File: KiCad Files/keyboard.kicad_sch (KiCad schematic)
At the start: 208 parts, among them J1 Conn_01x10, J2 Button, J3 78171-0004, J5 Conn_01x03_Male, U1 SOT-23-5 5.5V 3.3V 500mA, U2 RP2040, U3 TXS0101DCK, Y1 3225_4P 12MHz

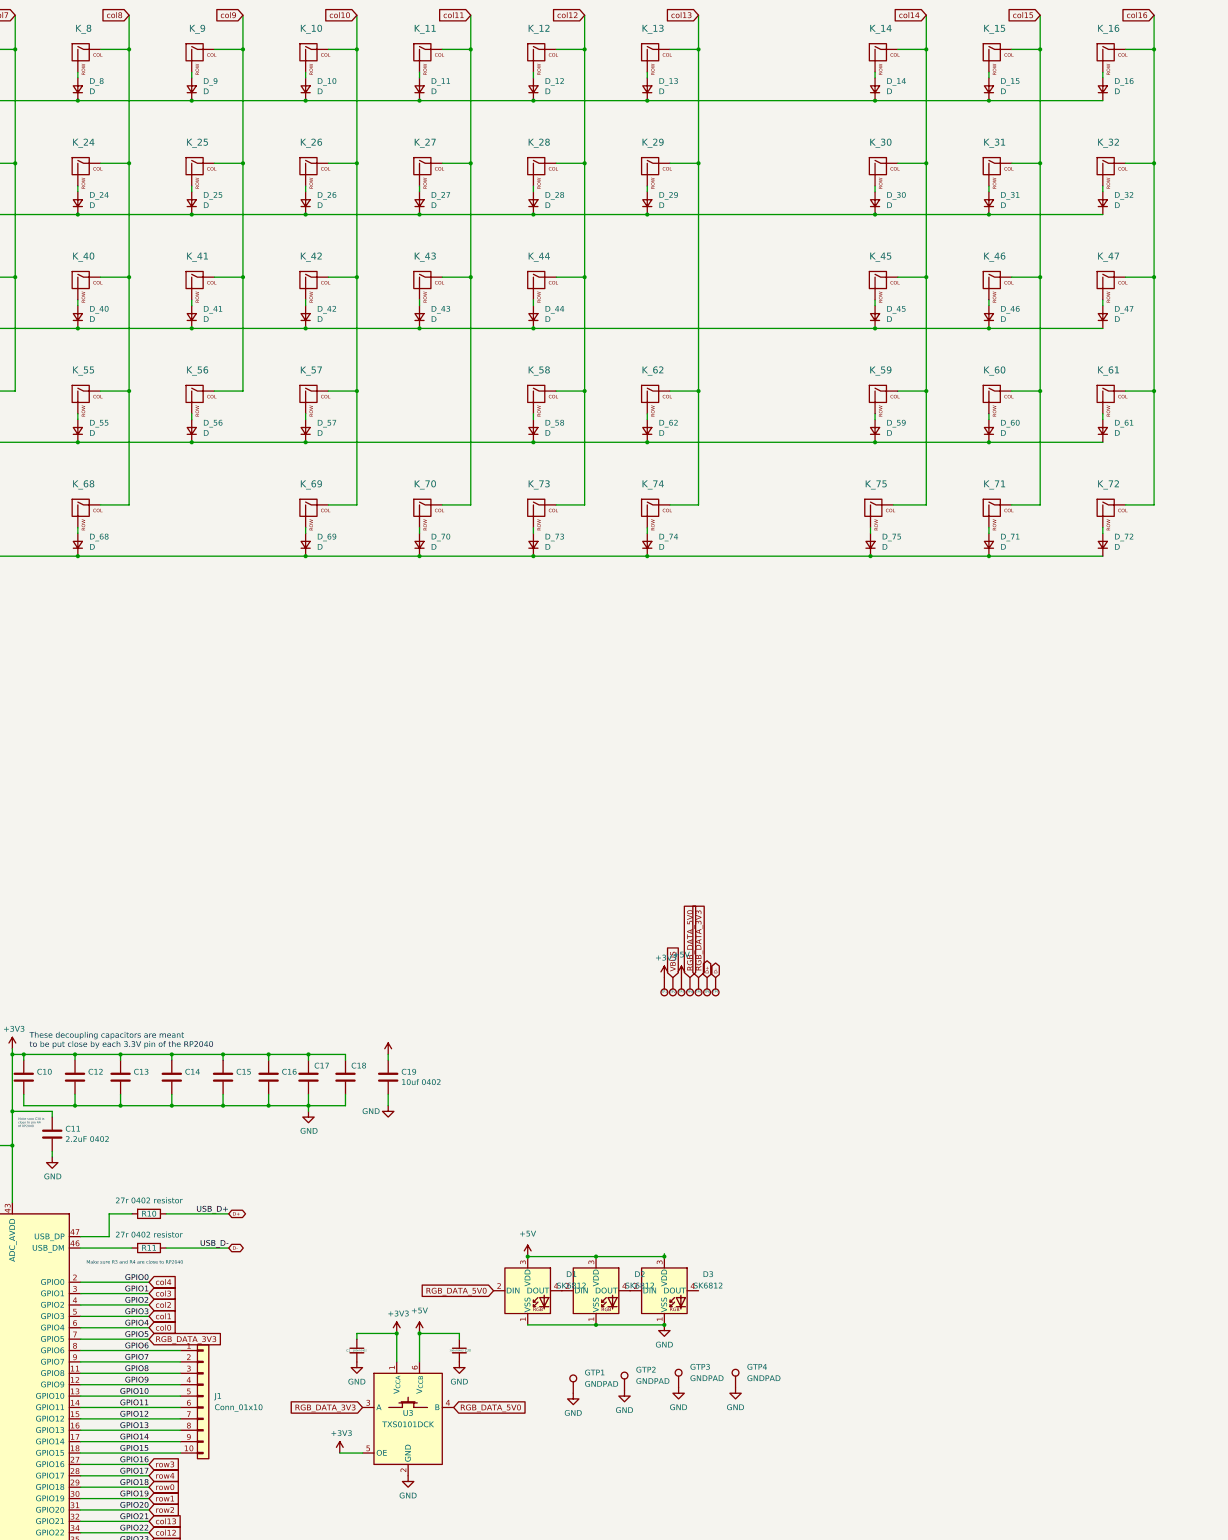
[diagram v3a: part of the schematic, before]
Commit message: corrected two major issues, columns 14,15 and 16 were not connected to any GPIOs, the LED footprints were incorrect for reverse mount.
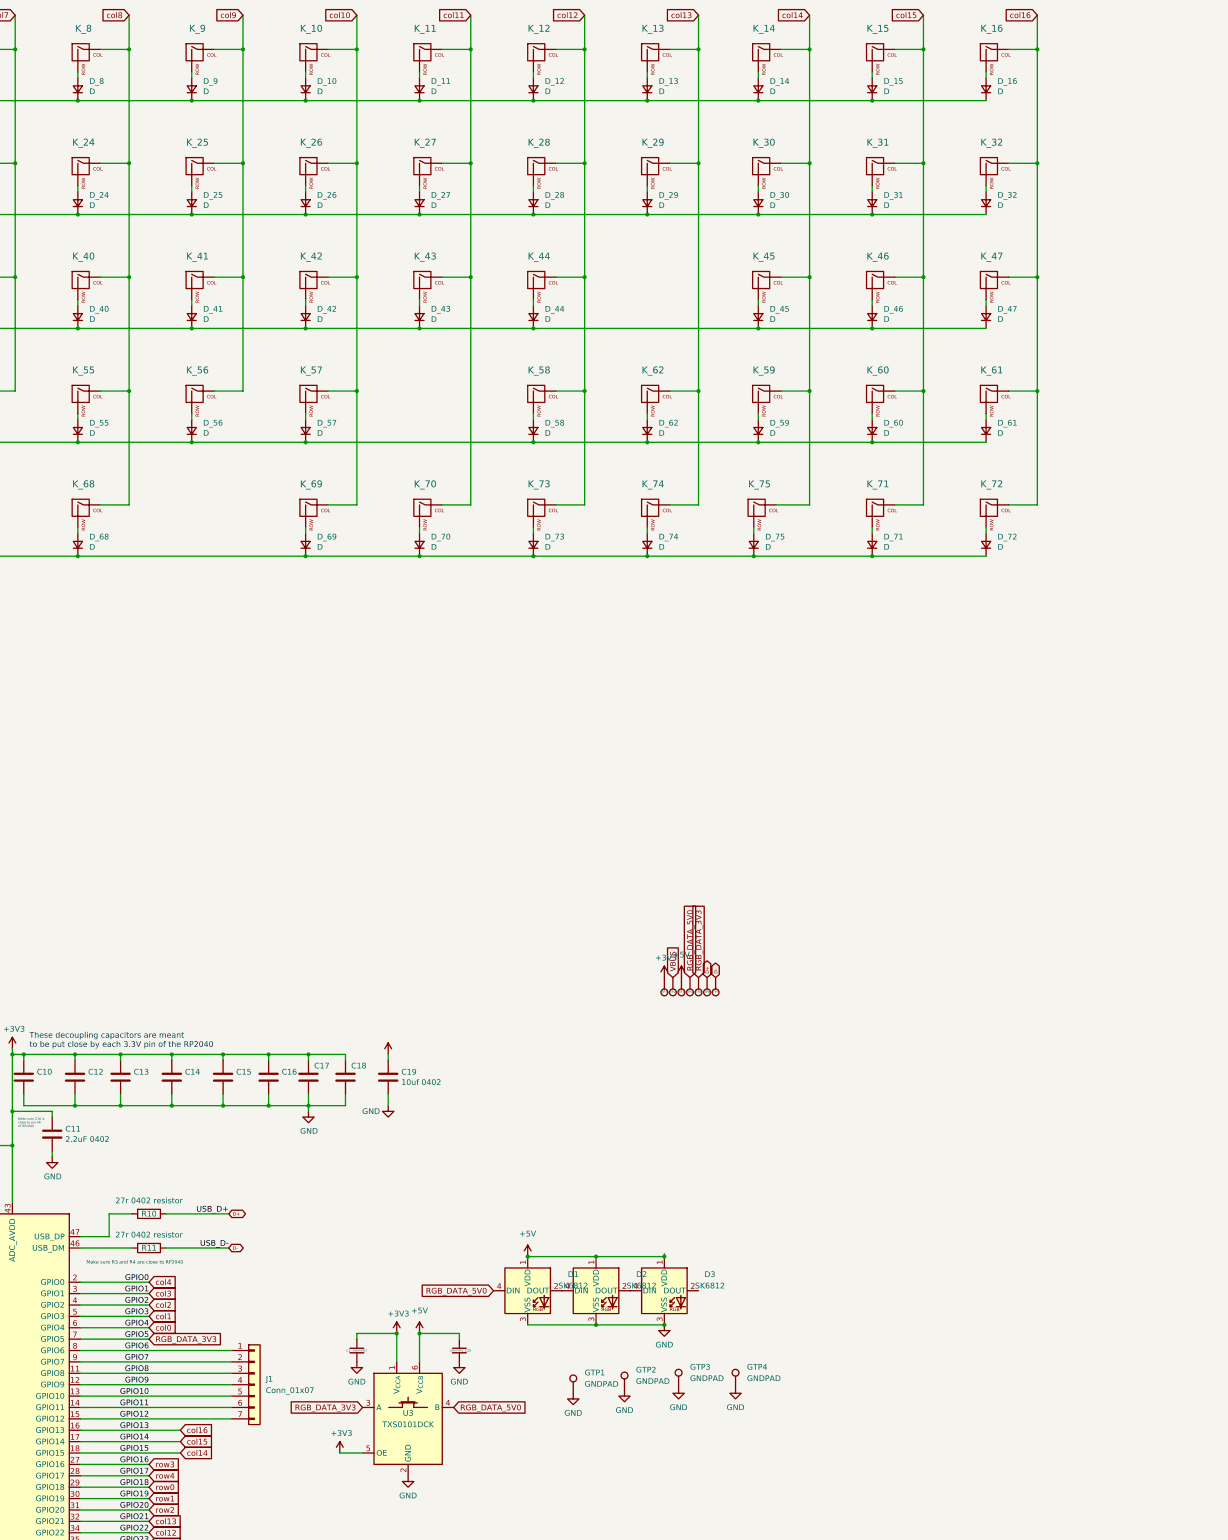
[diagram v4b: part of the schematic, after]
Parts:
- D1, D2, D3: footprint Keebio-Parts:SK6812-MINI-E -> sk6812mini:MX_SK6812MINI-E_REV; symbol LED:SK6812 -> LED:WS2812B
- J1: value Conn_01x10 -> Conn_01x07; footprint Connector_PinHeader_1.00mm:PinHeader_1x10_P1.00mm_Vertical -> Connector_PinHeader_1.00mm:PinHeader_1x07_P1.00mm_Vertical; symbol Connector_Generic:Conn_01x10 -> Connector_Generic:Conn_01x07
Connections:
- net +5V: now also D1.1 (VDD), D2.1 (VDD), D3.1 (VDD); no longer D1.3 (VDD), D2.3 (VDD), D3.3 (VDD)
- net GND: now also D1.3 (VSS), D2.3 (VSS), D3.3 (VSS); no longer D1.1 (VSS), D2.1 (VSS), D3.1 (VSS)
- net RGB_DATA_5V0: now also D1.4 (DIN); no longer D1.2 (DIN)
- net col14: now also U2.18 (GPIO15)
- net col15: now also U2.17 (GPIO14)
- net col16: now also U2.16 (GPIO13)
- net at D3.2 (DOUT): no longer D2.4 (DOUT)
- net at D3.4 (DIN): now also D2.2 (DOUT)
- removed net GPIO13: J1.8 (Pin_8), U2.16 (GPIO13)
- removed net GPIO14: J1.9 (Pin_9), U2.17 (GPIO14)
- removed net GPIO15: J1.10 (Pin_10), U2.18 (GPIO15)
- new net: D1.2 (DOUT), D2.4 (DIN)
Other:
- moved on the sheet: D_14, D_15, D_16, D_30, D_31, D_32, D_45, D_46, D_47, D_59, D_60, D_61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
